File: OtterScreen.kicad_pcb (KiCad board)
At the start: 2 copper layers, 44.8 x 31.4 mm, 27 parts, among them J1 47272-0001, J2 USB-C_Power, U1 5022505191, U2 NE555, U3 DIO5661, U4 DIO5661

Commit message: updated files
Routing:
- net HPD: track 30.4 -> 29.7 mm
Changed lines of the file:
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@@
-(kicad_pcb (version 20171130) (host pcbnew 5.1.2)
+(kicad_pcb (version 20171130) (host pcbnew 5.0.1)
   (general
     (thickness 1.6)
     (drawings 15)
-    (tracks 718)
+    (tracks 717)
     (zones 0)
     (modules 27)
@@
     (zone_45_only no)
     (trace_min 0.154)
+    (segment_width 0.2)
+    (edge_width 0.15)
     (via_size 0.6)
     (via_drill 0.3)
@@
     (uvia_min_size 0.2)
     (uvia_min_drill 0.1)
-    (edge_width 0.15)
-    (segment_width 0.2)
     (pcb_text_width 0.3)
     (pcb_text_size 1.5 1.5)
@@
     (uvia_dia 0.3)
     (uvia_drill 0.1)
+    (diff_pair_gap 0.2)
     (diff_pair_width 0.154)
-    (diff_pair_gap 0.2)
     (add_net +3V3)
     (add_net +5V)
@@
   (via (at 145.1 127.4) (size 0.6) (drill 0.3) (layers F.Cu B.Cu) (net 3))
   (segment (start 145.15 127.45) (end 145.1 127.4) (width 0.154) (layer F.Cu) (net 3))
-  (segment (start 152.3 116.195) (end 152.3 115.566) (width 0.154) (layer F.Cu) (net 3))
   (segment (start 152.853894 116.168989) (end 153.153893 115.86899) (width 0.154) (layer F.Cu) (net 3))
   (segment (start 152.827883 116.195) (end 152.853894 116.168989) (width 0.154) (layer F.Cu) (net 3))

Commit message: fixed bugs, added ams1117
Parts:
- removed G***: LOGO, otter:otter_wave_118
- added C10: 220nF, Capacitor_SMD:C_0603_1608Metric, F.Cu at (148.6, 119.8)
- added C11: 220nF, Capacitor_SMD:C_0603_1608Metric, F.Cu at (141.4, 121.7)
- added C8: 0.47uF, Capacitor_SMD:C_0805_2012Metric, F.Cu at (124.6, 130.6)
- added C9: 0.47uF, Capacitor_SMD:C_0805_2012Metric, F.Cu at (130.1, 121.5)
- added H1: MountingHole_Pad, MountingHole:MountingHole_3.2mm_M3, F.Cu at (125.0, 118.0)
- added H2: MountingHole_Pad, MountingHole:MountingHole_3.2mm_M3, F.Cu at (161.8, 118.0)
- added U5: AMS1117-3.3, Package_TO_SOT_SMD:SOT-223-3_TabPin2, F.Cu at (127.3, 126.0)
- R6, R7: value R8 -> 0.8
- U3, U4: value DIO5661 -> TPS61160A; footprint Package_TO_SOT_SMD:SOT-23-6 -> Package_SON:WSON-6-1EP_2x2mm_P0.65mm_EP1x1.6mm
- moved L2 30.3 mm to (154.9, 118.0), turned to 270 degrees
- moved C1 28.3 mm to (150.4, 143.8), turned to 270 degrees
- moved J2 28.2 mm to (156.5, 140.2)
- moved R2 27.0 mm to (162.3, 140.7), turned to 90 degrees
- moved R1 26.9 mm to (162.3, 143.7), turned to 270 degrees
- moved C6 25.7 mm to (151.0, 115.9), turned to 180 degrees
- moved D3 25.4 mm to (154.9, 121.4), turned to 0 degrees
- moved D1 23.7 mm to (146.6, 144.3), turned to 0 degrees
- moved U3 20.9 mm to (151.0, 118.1), turned to 0 degrees
- moved C4 19.6 mm to (144.7, 124.1), turned to 90 degrees
- moved C7 19.0 mm to (151.0, 120.3), turned to 180 degrees
- moved L1 18.4 mm to (142.6, 128.0), turned to 180 degrees
- moved R7 16.7 mm to (148.4, 116.6)
- moved U2 16.1 mm to (146.7, 139.7), turned to 0 degrees
- moved J1 15.5 mm to (132.7, 145.7)
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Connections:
- J1 pad 20: +3V3 -> Net-(J1-Pad20)
- U3 pad 1: Net-(D2-Pad2) -> LEDC2
- U3 pad 2: GND -> Net-(C10-Pad1)
- U3 pad 3: LEDC1 -> GND
- U3 pad 4: PWM -> Net-(D3-Pad2)
- U3 pad 5: Net-(U3-Pad5) -> PWM
- U4 pad 1: Net-(D3-Pad2) -> LEDC1
- U4 pad 2: GND -> Net-(C11-Pad1)
- U4 pad 3: LEDC2 -> GND
- U4 pad 4: PWM -> Net-(D2-Pad2)
- U4 pad 5: Net-(U4-Pad5) -> PWM
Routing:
- net +5V: track 59.5 -> 120.1 mm, vias 0 -> 3
- net Net-(D1-Pad2): track 46.0 -> 14.8 mm, vias 2 -> 0
- net Net-(R5-Pad2): track 34.2 -> 8.12 mm, vias 2 -> 0
- net +3V3: track 36.0 -> 11.3 mm, vias 4 -> 3
- net Net-(C3-Pad1): track 57.3 -> 33.4 mm, vias 4 -> 0
- net PWM: track 22.2 -> 45.8 mm, vias 3 -> 4
- net AUX_N: track 31.6 -> 14.0 mm, vias 2 -> 0
- net HPD: track 29.7 -> 13.2 mm
- net AUX_P: track 30.8 -> 16.7 mm
- net LEDC1: track 18.8 -> 10.8 mm
- net L0_N: track 19.6 -> 13.3 mm
- net L0_P: track 19.6 -> 13.4 mm, vias 2 -> 0
- net L1_P: track 19.5 -> 13.2 mm, vias 2 -> 0
- net L1_N: track 19.7 -> 13.5 mm
- net L3_P: track 19.5 -> 13.4 mm
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- added copper zone on B.Cu, net +3V3
- added copper zone on F.Cu, net +3V3
- removed copper zone on F.Cu, net Net-(D2-Pad2)
- removed copper zone on F.Cu, net Net-(D3-Pad2)
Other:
- board text added: "Otter- Screen- Adapter"
- board text removed: "OtterScreen- Adapter"

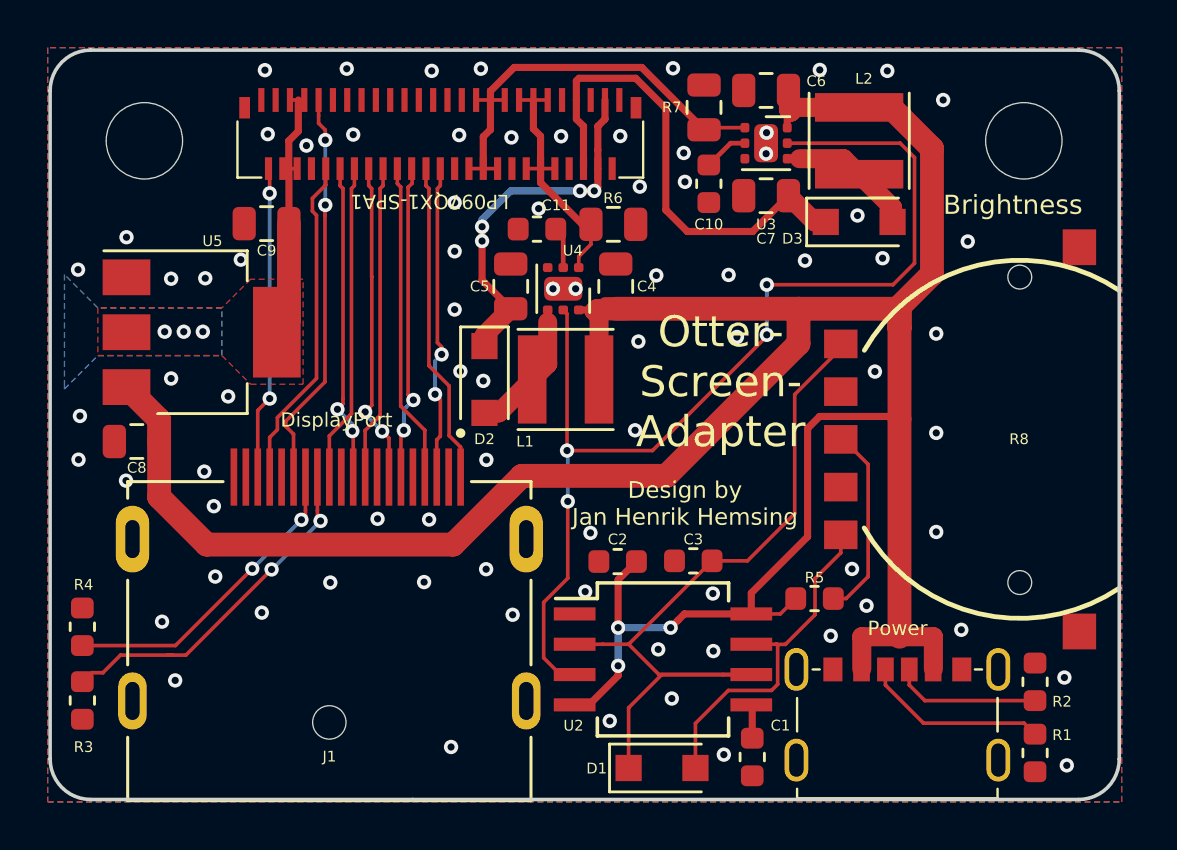
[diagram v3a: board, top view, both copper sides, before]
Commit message: fixed otter-screen-adapter, added gerber
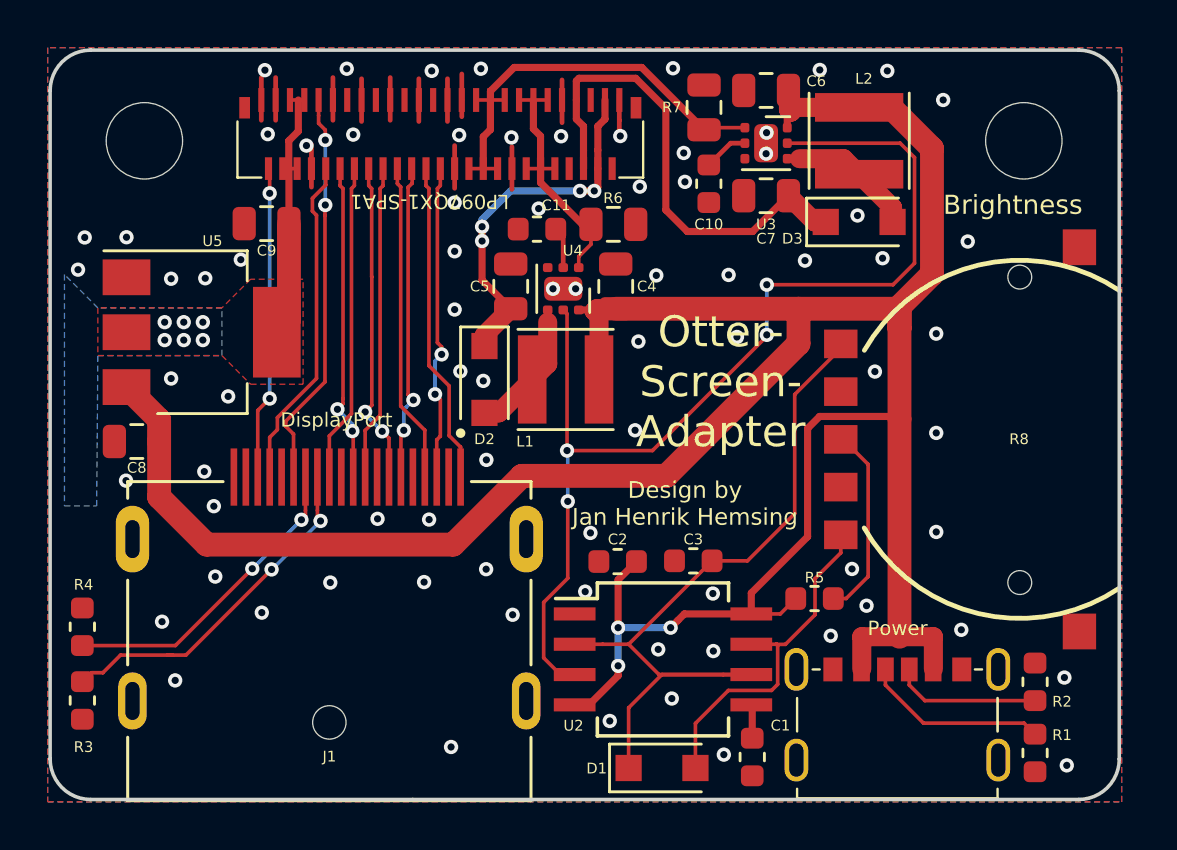
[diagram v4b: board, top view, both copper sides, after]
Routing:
- net GND: track 0.00 -> 23.3 mm, vias 79 -> 78
- net +3V3: vias 3 -> 6
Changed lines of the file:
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@@
-(kicad_pcb (version 20171130) (host pcbnew 5.0.1)
+(kicad_pcb (version 20171130) (host pcbnew 5.1.4+dfsg1-1)
   (general
     (thickness 1.6)
     (drawings 17)
-    (tracks 413)
+    (tracks 441)
     (zones 0)
     (modules 33)
@@
   )
   (setup
-    (last_trace_width 0.154)
+    (last_trace_width 0.2)
     (user_trace_width 0.154)
     (user_trace_width 0.3)
@@
     (zone_45_only yes)
     (trace_min 0.154)
-    (segment_width 0.2)
-    (edge_width 0.15)
     (via_size 0.6)
     (via_drill 0.3)
@@
     (uvia_min_size 0.2)
     (uvia_min_drill 0.1)
+    (edge_width 0.15)
+    (segment_width 0.2)
     (pcb_text_width 0.3)
     (pcb_text_size 1.5 1.5)
@@
     (uvia_dia 0.3)
     (uvia_drill 0.1)
+    (diff_pair_width 0.154)
     (diff_pair_gap 0.2)
-    (diff_pair_width 0.154)
     (add_net +3V3)
     (add_net +5V)
@@
   (gr_line (start 121 143.9) (end 121.000001 115.900001) (layer Edge.Cuts) (width 0.15))
   (gr_line (start 136.2 145.6) (end 122.700001 145.599999) (layer Edge.Cuts) (width 0.15))
+  (via (at 125.8 126.35) (size 0.6) (drill 0.3) (layers F.Cu B.Cu) (net 2))
+  (via (at 126.6 126.35) (size 0.6) (drill 0.3) (layers F.Cu B.Cu) (net 2))
+  (via (at 127.4 126.35) (size 0.6) (drill 0.3) (layers F.Cu B.Cu) (net 2))
+  (segment (start 130.45 116.44) (end 130.45 117.14) (width 0.2) (layer F.Cu) (net 1))
+  (segment (start 130.45 116.44) (end 130.45 115.35) (width 0.2) (layer F.Cu) (net 1))
+  (segment (start 142.45 116.54) (end 142.45 117.24) (width 0.2) (layer F.Cu) (net 1))
+  (segment (start 142.45 116.54) (end 142.45 115.45) (width 0.2) (layer F.Cu) (net 1))
+  (segment (start 144.85 117.14) (end 144.85 117.84) (width 0.2) (layer F.Cu) (net 1))
+  (segment (start 144.85 117.14) (end 144.85 116.05) (width 0.2) (layer F.Cu) (net 1))
+  (segment (start 140.35 119.34) (end 140.35 120.04) (width 0.2) (layer F.Cu) (net 1))
+  (segment (start 140.35 119.34) (end 140.35 118.25) (width 0.2) (layer F.Cu) (net 1))
+  (segment (start 137.95 119.29) (end 137.95 119.99) (width 0.2) (layer F.Cu) (net 1))
+  (segment (start 137.95 119.29) (end 137.95 118.2) (width 0.2) (layer F.Cu) (net 1))
+  (segment (start 131.95 119.24) (end 131.95 119.94) (width 0.2) (layer F.Cu) (net 1))
+  (segment (start 131.95 119.24) (end 131.95 118.15) (width 0.2) (layer F.Cu) (net 1))
+  (segment (start 129.85 116.44) (end 129.85 117.14) (width 0.2) (layer F.Cu) (net 1))
+  (segment (start 129.85 116.44) (end 129.85 115.35) (width 0.2) (layer F.Cu) (net 1))
+  (segment (start 134.05 116.49) (end 134.05 117.19) (width 0.2) (layer F.Cu) (net 1))
+  (segment (start 134.05 116.49) (end 134.05 115.4) (width 0.2) (layer F.Cu) (net 1))
+  (segment (start 132.85 116.44) (end 132.85 117.14) (width 0.2) (layer F.Cu) (net 1))
+  (segment (start 132.85 116.44) (end 132.85 115.35) (width 0.2) (layer F.Cu) (net 1))
+  (segment (start 135.25 116.44) (end 135.25 117.14) (width 0.2) (layer F.Cu) (net 1))
+  (segment (start 135.25 116.44) (end 135.25 115.35) (width 0.2) (layer F.Cu) (net 1))
+  (segment (start 136.45 116.49) (end 136.45 117.19) (width 0.2) (layer F.Cu) (net 1))
+  (segment (start 136.45 116.49) (end 136.45 115.4) (width 0.2) (layer F.Cu) (net 1))
+  (segment (start 137.65 116.49) (end 137.65 117.19) (width 0.2) (layer F.Cu) (net 1))
+  (segment (start 137.65 116.49) (end 137.65 115.4) (width 0.2) (layer F.Cu) (net 1))
   (via (at 143.02 124.2) (size 0.6) (drill 0.3) (layers F.Cu B.Cu) (net 1))
   (via (at 142.07 124.2) (size 0.6) (drill 0.3) (layers F.Cu B.Cu) (net 1))
@@
   (via (at 127.86 133.31) (size 0.6) (drill 0.3) (layers F.Cu B.Cu) (net 1))
   (via (at 124.18 132.24) (size 0.6) (drill 0.3) (layers F.Cu B.Cu) (net 1))
-  (via (at 122.25 129.53) (size 0.6) (drill 0.3) (layers F.Cu B.Cu) (net 1))
-  (via (at 122.19 131.36) (size 0.6) (drill 0.3) (layers F.Cu B.Cu) (net 1))
   (via (at 127.92 136.26) (size 0.6) (drill 0.3) (layers F.Cu B.Cu) (net 1))
   (via (at 125.69 138.15) (size 0.6) (drill 0.3) (layers F.Cu B.Cu) (net 1))
@@
   (via (at 147.55 118.51) (size 0.6) (drill 0.3) (layers F.Cu B.Cu) (net 1))
   (via (at 141.47 120.84) (size 0.6) (drill 0.3) (layers F.Cu B.Cu) (net 1))
-  (via (at 125.8 126) (size 0.6) (drill 0.3) (layers F.Cu B.Cu) (net 2))
-  (via (at 126.6 126) (size 0.6) (drill 0.3) (layers F.Cu B.Cu) (net 2))
-  (via (at 127.4 126) (size 0.6) (drill 0.3) (layers F.Cu B.Cu) (net 2))
+  (segment (start 138.25 116.29) (end 138.25 116.99) (width 0.2) (layer F.Cu) (net 1))
+  (segment (start 138.25 116.29) (end 138.25 115.2) (width 0.2) (layer F.Cu) (net 1))
+  (via (at 122.45 122.05) (size 0.6) (drill 0.3) (layers F.Cu B.Cu) (net 1))
+  (via (at 125.8 125.6) (size 0.6) (drill 0.3) (layers F.Cu B.Cu) (net 2))
+  (via (at 126.6 125.6) (size 0.6) (drill 0.3) (layers F.Cu B.Cu) (net 2))
+  (via (at 127.4 125.6) (size 0.6) (drill 0.3) (layers F.Cu B.Cu) (net 2))
   (segment (start 131.4 116.29) (end 131.05 116.29) (width 0.154) (layer F.Cu) (net 2))
   (segment (start 131.65 116.29) (end 131.4 116.29) (width 0.154) (layer F.Cu) (net 2))
@@
     (polygon
       (pts
-        (xy 128.2 125) (xy 123 125) (xy 121.6 123.6) (xy 121.6 128.2) (xy 121.6 128.4)
+        (xy 128.2 125) (xy 123 125) (xy 121.6 123.6) (xy 121.6 133.3) (xy 122.95 133.3)
         (xy 123 127) (xy 128.2 127)
       )
@@
       )
     )
+  )
+  (zone (net 0) (net_name "") (layer F.Cu) (hatch edge 0.508)
+    (connect_pads (clearance 0.2))
+    (min_thickness 0.254)
+    (keepout (tracks allowed) (vias allowed) (copperpour not_allowed))
+    (fill (arc_segments 32) (thermal_gap 0.508) (thermal_bridge_width 0.508))
+    (polygon
+      (pts
+        (xy 129.5 115.6) (xy 129.5 117) (xy 145.1 117) (xy 145.1 115.6)
+      )
+    )
+  )
+  (zone (net 0) (net_name "") (layer F.Cu) (hatch edge 0.508)
+    (connect_pads (clearance 0.2))
+    (min_thickness 0.254)
+    (keepout (tracks allowed) (vias allowed) (copperpour not_allowed))
+    (fill (arc_segments 32) (thermal_gap 0.508) (thermal_bridge_width 0.508))
+    (polygon
+      (pts
+        (xy 129.5 118.5) (xy 129.5 119.9) (xy 145.1 119.9) (xy 145.1 118.5)
+      )
+    )
